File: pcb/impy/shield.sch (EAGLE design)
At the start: 119 parts, among them J1 USB-2410-06, J2 SI-60062-F, J3 5V, U1 AD5933YRS, U10 LTC3406AB, U11 23LCV1024-I/SN, U12 MIC2009A-1YM6, U13 ADG725BSU, U14 ADG725BSU, U2 ADG704BRM, U3 AD8656ARZ, U4 M24C08WMN, U5 ADG706BRU, U6 DP83848I, U7 MIC2009A-1YM6, U8 AT25DF081A-SS, U9 SST25VF080B-80-4I-S2

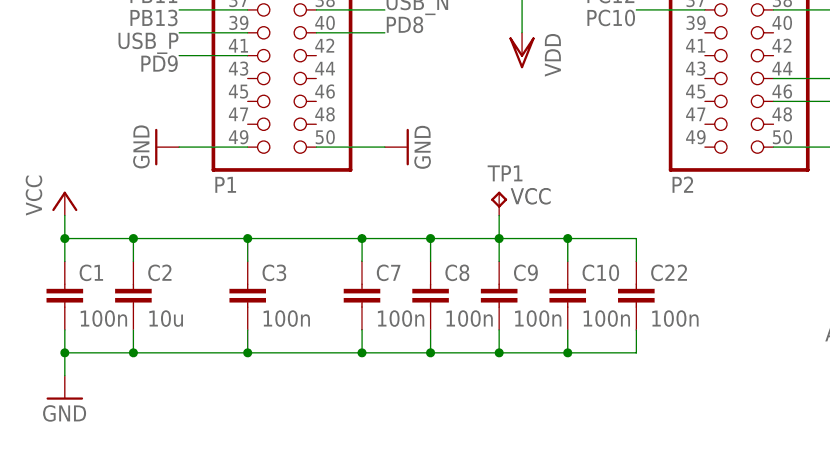
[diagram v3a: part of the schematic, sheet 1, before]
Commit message: * pcb/impy: (shield.brd) Layout USB connector.   (shield.sch) Fix wrong supply net connection for USB bypass capacitors C1 and C2 (was VCC, should be +5V).
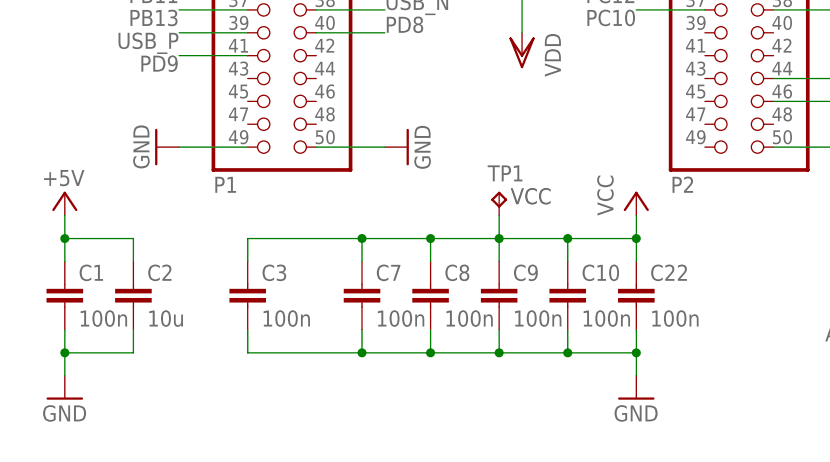
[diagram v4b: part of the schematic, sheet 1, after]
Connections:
- net +5V: now also C1.1, C2.1
- net VCC: no longer C1.1, C2.1
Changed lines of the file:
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@@
 </part>
 <part name="R20" library="rcl" deviceset="R-EU_" device="R0603" value="10k"/>
+<part name="GND44" library="supply1" deviceset="GND" device=""/>
+<part name="P+36" library="supply1" deviceset="+5V" device=""/>
 </parts>
 <sheets>
@@
 <instance part="C6" gate="G$1" x="114.3" y="5.08"/>
 <instance part="GND14" gate="1" x="0" y="-7.62"/>
-<instance part="P+12" gate="VCC" x="0" y="15.24"/>
+<instance part="P+12" gate="VCC" x="63.5" y="15.24"/>
 <instance part="P+13" gate="VCC" x="104.14" y="15.24"/>
 <instance part="AGND6" gate="VR1" x="104.14" y="-7.62"/>
@@
 <instance part="TP1" gate="G$1" x="48.26" y="15.24"/>
 <instance part="TP2" gate="G$1" x="152.4" y="25.4"/>
+<instance part="GND44" gate="1" x="63.5" y="-7.62"/>
+<instance part="P+36" gate="1" x="0" y="15.24" smashed="yes" rot="MR0">
+<attribute name="VALUE" x="-2.54" y="17.78" size="1.778" layer="96" rot="MR180"/>
+</instance>
 </instances>
 <busses>
@@
 </segment>
 <segment>
-<pinref part="C1" gate="G$1" pin="2"/>
+<pinref part="C2" gate="G$1" pin="2"/>
+<wire x1="7.62" y1="-2.54" x2="7.62" y2="0" width="0.1524" layer="91"/>
 <pinref part="GND14" gate="1" pin="GND"/>
-<wire x1="0" y1="0" x2="0" y2="-2.54" width="0.1524" layer="91"/>
-<pinref part="C2" gate="G$1" pin="2"/>
 <wire x1="0" y1="-2.54" x2="0" y2="-5.08" width="0.1524" layer="91"/>
 <wire x1="0" y1="-2.54" x2="7.62" y2="-2.54" width="0.1524" layer="91"/>
-<wire x1="7.62" y1="-2.54" x2="7.62" y2="0" width="0.1524" layer="91"/>
 <junction x="0" y="-2.54"/>
+<pinref part="C1" gate="G$1" pin="2"/>
+<wire x1="0" y1="0" x2="0" y2="-2.54" width="0.1524" layer="91"/>
+</segment>
+<segment>
 <pinref part="C3" gate="G$1" pin="2"/>
-<wire x1="7.62" y1="-2.54" x2="20.32" y2="-2.54" width="0.1524" layer="91"/>
 <wire x1="20.32" y1="-2.54" x2="20.32" y2="0" width="0.1524" layer="91"/>
-<junction x="7.62" y="-2.54"/>
 <pinref part="C7" gate="G$1" pin="2"/>
 <wire x1="20.32" y1="-2.54" x2="33.02" y2="-2.54" width="0.1524" layer="91"/>
 <wire x1="33.02" y1="-2.54" x2="33.02" y2="0" width="0.1524" layer="91"/>
-<junction x="20.32" y="-2.54"/>
 <pinref part="C8" gate="G$1" pin="2"/>
 <wire x1="33.02" y1="-2.54" x2="40.64" y2="-2.54" width="0.1524" layer="91"/>
@@
 <wire x1="63.5" y1="-2.54" x2="63.5" y2="0" width="0.1524" layer="91"/>
 <junction x="55.88" y="-2.54"/>
+<pinref part="GND44" gate="1" pin="GND"/>
+<wire x1="63.5" y1="-5.08" x2="63.5" y2="-2.54" width="0.1524" layer="91"/>
+<junction x="63.5" y="-2.54"/>
 </segment>
 <segment>
@@
 <junction x="96.52" y="78.74"/>
 </segment>
+<segment>
+<pinref part="C1" gate="G$1" pin="1"/>
+<pinref part="C2" gate="G$1" pin="1"/>
+<wire x1="7.62" y1="10.16" x2="7.62" y2="7.62" width="0.1524" layer="91"/>
+<wire x1="0" y1="10.16" x2="7.62" y2="10.16" width="0.1524" layer="91"/>
+<wire x1="0" y1="10.16" x2="0" y2="7.62" width="0.1524" layer="91"/>
+<pinref part="P+36" gate="1" pin="+5V"/>
+<wire x1="0" y1="10.16" x2="0" y2="12.7" width="0.1524" layer="91"/>
+<junction x="0" y="10.16"/>
+</segment>
 </net>
 <net name="+3V3" class="1">
@@
 <segment>
 <pinref part="P+12" gate="VCC" pin="VCC"/>
-<pinref part="C1" gate="G$1" pin="1"/>
-<wire x1="0" y1="12.7" x2="0" y2="10.16" width="0.1524" layer="91"/>
-<pinref part="C2" gate="G$1" pin="1"/>
-<wire x1="0" y1="10.16" x2="0" y2="7.62" width="0.1524" layer="91"/>
-<wire x1="0" y1="10.16" x2="7.62" y2="10.16" width="0.1524" layer="91"/>
-<wire x1="7.62" y1="10.16" x2="7.62" y2="7.62" width="0.1524" layer="91"/>
-<junction x="0" y="10.16"/>
 <pinref part="C3" gate="G$1" pin="1"/>
-<wire x1="7.62" y1="10.16" x2="20.32" y2="10.16" width="0.1524" layer="91"/>
 <wire x1="20.32" y1="10.16" x2="20.32" y2="7.62" width="0.1524" layer="91"/>
-<junction x="7.62" y="10.16"/>
 <pinref part="C7" gate="G$1" pin="1"/>
 <wire x1="20.32" y1="10.16" x2="33.02" y2="10.16" width="0.1524" layer="91"/>
 <wire x1="33.02" y1="10.16" x2="33.02" y2="7.62" width="0.1524" layer="91"/>
-<junction x="20.32" y="10.16"/>
 <pinref part="C8" gate="G$1" pin="1"/>
 <wire x1="33.02" y1="10.16" x2="40.64" y2="10.16" width="0.1524" layer="91"/>
@@
 <pinref part="TP1" gate="G$1" pin="TP"/>
 <wire x1="48.26" y1="12.7" x2="48.26" y2="10.16" width="0.1524" layer="91"/>
-</segment>
-<segment>
+<wire x1="63.5" y1="10.16" x2="63.5" y2="12.7" width="0.1524" layer="91"/>
+<junction x="63.5" y="10.16"/>
+</segment>
+<segment>

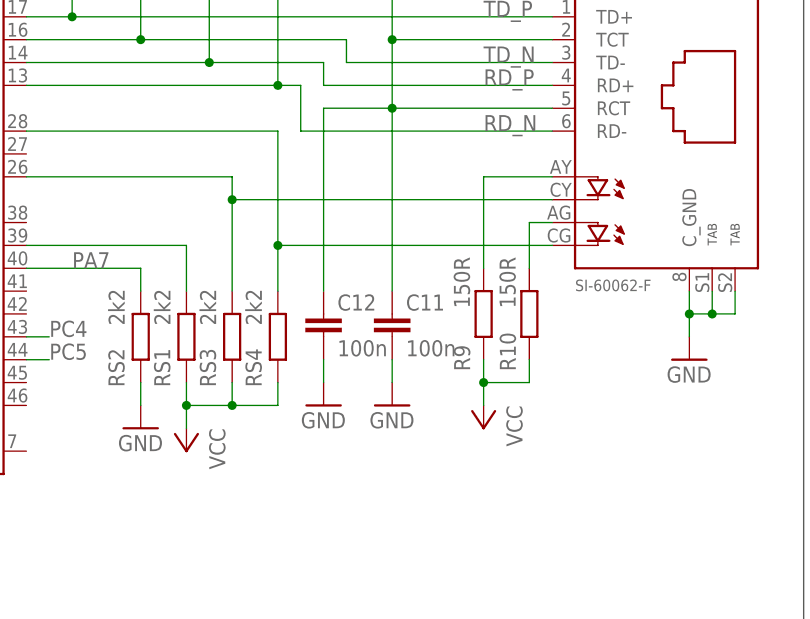
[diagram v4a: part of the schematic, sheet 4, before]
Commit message: * pcb/impy: (shield.sch) Swap around Ethernet jack LED dropper resistors for better routing.   (shield.brd) Change layout of Ethernet LEDs.
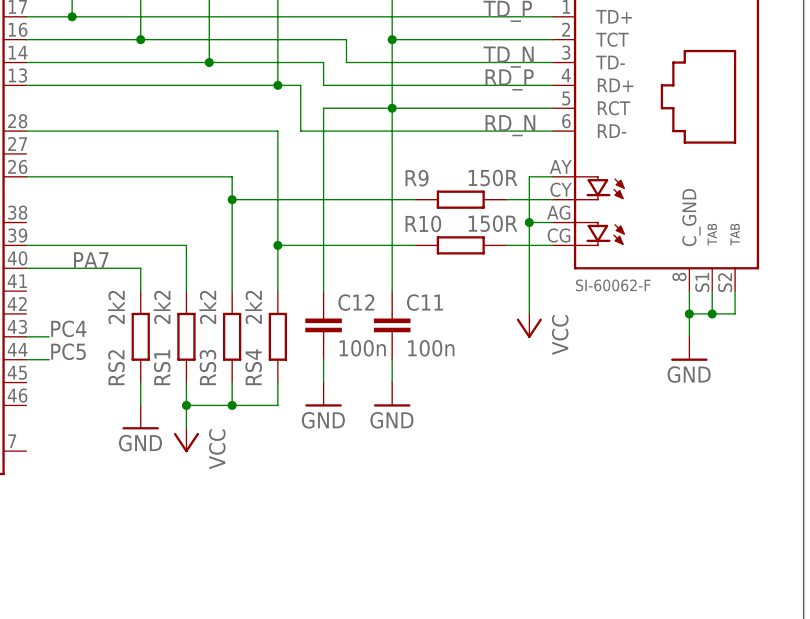
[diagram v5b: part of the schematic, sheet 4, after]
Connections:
- net N$20: now also J2.CY, R9.2; no longer J2.AG, R10.2
- net N$22: now also R9.1; no longer J2.CY
- net N$23: now also R10.1; no longer J2.CG
- net N$25: now also J2.CG, R10.2; no longer J2.AY, R9.2
- net VCC: now also J2.AG, J2.AY; no longer R10.1, R9.1
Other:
- moved on the sheet: R10, R9
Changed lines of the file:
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@@
 </instance>
 <instance part="GND30" gate="1" x="119.38" y="78.74" rot="R180"/>
-<instance part="P+23" gate="VCC" x="187.96" y="20.32" rot="R180"/>
+<instance part="P+23" gate="VCC" x="193.04" y="30.48" rot="R180"/>
 <instance part="RS3" gate="G$1" x="160.02" y="30.48" smashed="yes" rot="R90">
 <attribute name="NAME" x="156.4386" y="29.21" size="1.778" layer="95" rot="R270"/>
@@
 <attribute name="VALUE" x="163.322" y="31.75" size="1.778" layer="96" rot="R90"/>
 </instance>
-<instance part="R9" gate="G$1" x="187.96" y="33.02" smashed="yes" rot="R90">
-<attribute name="NAME" x="186.4614" y="26.67" size="1.778" layer="95" rot="R90"/>
-<attribute name="VALUE" x="184.658" y="39.37" size="1.778" layer="96" rot="R270"/>
+<instance part="R9" gate="G$1" x="185.42" y="45.72" smashed="yes">
+<attribute name="NAME" x="179.07" y="47.2186" size="1.778" layer="95"/>
+<attribute name="VALUE" x="191.77" y="49.022" size="1.778" layer="96" rot="R180"/>
 </instance>
-<instance part="R10" gate="G$1" x="193.04" y="33.02" smashed="yes" rot="R90">
-<attribute name="NAME" x="191.5414" y="26.67" size="1.778" layer="95" rot="R90"/>
-<attribute name="VALUE" x="189.738" y="39.37" size="1.778" layer="96" rot="R270"/>
+<instance part="R10" gate="G$1" x="185.42" y="40.64" smashed="yes">
+<attribute name="NAME" x="179.07" y="42.1386" size="1.778" layer="95"/>
+<attribute name="VALUE" x="191.77" y="43.942" size="1.778" layer="96" rot="R180"/>
 </instance>
 <instance part="U7" gate="G$1" x="10.16" y="35.56"/>
@@
 </segment>
 <segment>
-<pinref part="P+23" gate="VCC" pin="VCC"/>
-<pinref part="R9" gate="G$1" pin="1"/>
-<wire x1="187.96" y1="22.86" x2="187.96" y2="25.4" width="0.1524" layer="91"/>
-<pinref part="R10" gate="G$1" pin="1"/>
-<wire x1="187.96" y1="25.4" x2="187.96" y2="27.94" width="0.1524" layer="91"/>
-<wire x1="187.96" y1="25.4" x2="193.04" y2="25.4" width="0.1524" layer="91"/>
-<wire x1="193.04" y1="25.4" x2="193.04" y2="27.94" width="0.1524" layer="91"/>
-<junction x="187.96" y="25.4"/>
-</segment>
-<segment>
 <pinref part="R11" gate="G$1" pin="2"/>
 <pinref part="P+30" gate="VCC" pin="VCC"/>
 <wire x1="43.18" y1="38.1" x2="43.18" y2="40.64" width="0.1524" layer="91"/>
+</segment>
+<segment>
+<pinref part="J2" gate="G$1" pin="AY"/>
+<pinref part="P+23" gate="VCC" pin="VCC"/>
+<wire x1="195.58" y1="48.26" x2="193.04" y2="48.26" width="0.1524" layer="91"/>
+<wire x1="193.04" y1="48.26" x2="193.04" y2="43.18" width="0.1524" layer="91"/>
+<pinref part="J2" gate="G$1" pin="AG"/>
+<wire x1="193.04" y1="43.18" x2="193.04" y2="33.02" width="0.1524" layer="91"/>
+<wire x1="195.58" y1="43.18" x2="193.04" y2="43.18" width="0.1524" layer="91"/>
+<junction x="193.04" y="43.18"/>
 </segment>
 </net>
@@
 <wire x1="137.16" y1="48.26" x2="160.02" y2="48.26" width="0.1524" layer="91"/>
 <wire x1="160.02" y1="48.26" x2="160.02" y2="45.72" width="0.1524" layer="91"/>
-<pinref part="J2" gate="G$1" pin="CY"/>
+<pinref part="R9" gate="G$1" pin="1"/>
 <wire x1="160.02" y1="45.72" x2="160.02" y2="35.56" width="0.1524" layer="91"/>
-<wire x1="195.58" y1="45.72" x2="160.02" y2="45.72" width="0.1524" layer="91"/>
+<wire x1="180.34" y1="45.72" x2="160.02" y2="45.72" width="0.1524" layer="91"/>
 <junction x="160.02" y="45.72"/>
 </segment>
@@
 <wire x1="137.16" y1="53.34" x2="165.1" y2="53.34" width="0.1524" layer="91"/>
 <wire x1="165.1" y1="53.34" x2="165.1" y2="40.64" width="0.1524" layer="91"/>
-<pinref part="J2" gate="G$1" pin="CG"/>
+<pinref part="R10" gate="G$1" pin="1"/>
 <wire x1="165.1" y1="40.64" x2="165.1" y2="35.56" width="0.1524" layer="91"/>
-<wire x1="195.58" y1="40.64" x2="165.1" y2="40.64" width="0.1524" layer="91"/>
+<wire x1="180.34" y1="40.64" x2="165.1" y2="40.64" width="0.1524" layer="91"/>
 <junction x="165.1" y="40.64"/>
-</segment>
-</net>
-<net name="N$20" class="0">
-<segment>
-<pinref part="J2" gate="G$1" pin="AG"/>
-<pinref part="R10" gate="G$1" pin="2"/>
-<wire x1="195.58" y1="43.18" x2="193.04" y2="43.18" width="0.1524" layer="91"/>
-<wire x1="193.04" y1="43.18" x2="193.04" y2="38.1" width="0.1524" layer="91"/>
-</segment>
-</net>
-<net name="N$25" class="0">
-<segment>
-<pinref part="J2" gate="G$1" pin="AY"/>
-<pinref part="R9" gate="G$1" pin="2"/>
-<wire x1="195.58" y1="48.26" x2="187.96" y2="48.26" width="0.1524" layer="91"/>
-<wire x1="187.96" y1="48.26" x2="187.96" y2="38.1" width="0.1524" layer="91"/>
 </segment>
 </net>
@@
 </segment>
 </net>
+<net name="N$20" class="0">
+<segment>
+<pinref part="R9" gate="G$1" pin="2"/>
+<pinref part="J2" gate="G$1" pin="CY"/>
+<wire x1="190.5" y1="45.72" x2="195.58" y2="45.72" width="0.1524" layer="91"/>
+</segment>
+</net>
+<net name="N$25" class="0">
+<segment>
+<pinref part="J2" gate="G$1" pin="CG"/>
+<pinref part="R10" gate="G$1" pin="2"/>
+<wire x1="195.58" y1="40.64" x2="190.5" y2="40.64" width="0.1524" layer="91"/>
+</segment>
+</net>

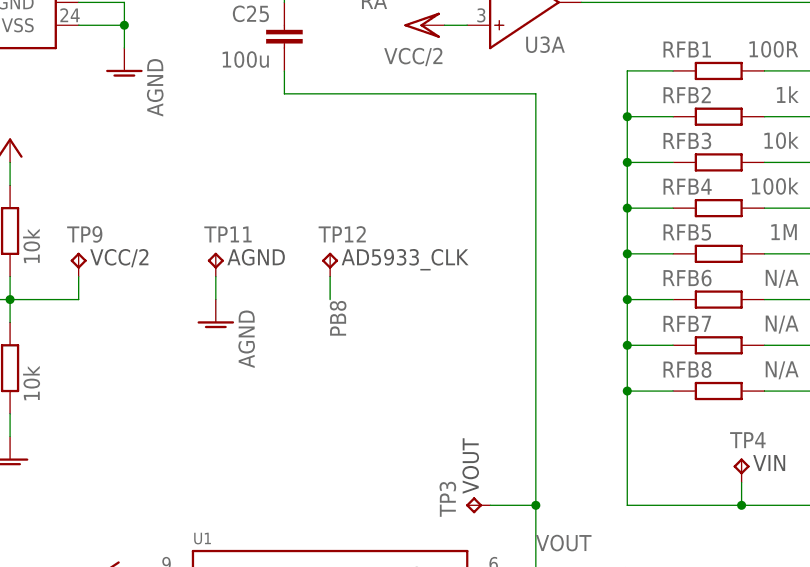
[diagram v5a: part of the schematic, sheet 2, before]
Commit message: * pcb/impy: (shield.brd) Layout most of the AD5933 related circuit.   (shield.sch) Remove unnecessary AD5933 clock signal test pad (TP12), is accessible from the discovery board anyway.
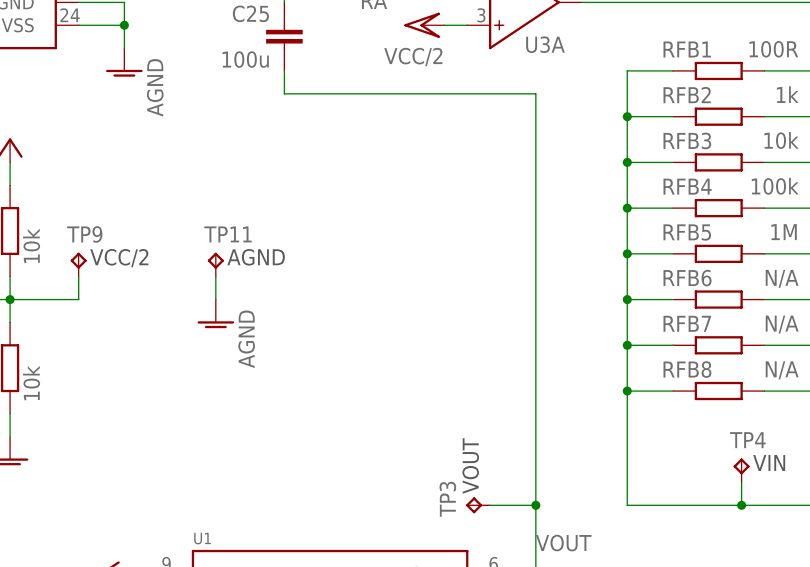
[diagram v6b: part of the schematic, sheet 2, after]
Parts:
- removed TP12: TPTP20R, testpad:TPTP20R
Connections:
- net PB8: no longer TP12.TP
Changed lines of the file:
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@@
 <attribute name="TP_SIGNAL_NAME" value="MAC_CLK"/>
-</part>
-<part name="TP12" library="testpad" deviceset="TP" device="TP20R">
-<attribute name="TP_SIGNAL_NAME" value="AD5933_CLK"/>
 </part>
 <part name="R20" library="rcl" deviceset="R-EU_" device="R0603" value="10k"/>
@@
 <instance part="TP11" gate="G$1" x="35.56" y="88.9"/>
 <instance part="AGND14" gate="VR1" x="35.56" y="81.28" rot="MR0"/>
-<instance part="TP12" gate="G$1" x="48.26" y="88.9"/>
 <instance part="R20" gate="G$1" x="147.32" y="58.42"/>
 </instances>
@@
 <label x="22.86" y="40.64" size="1.778" layer="95" rot="R180"/>
 </segment>
-<segment>
-<pinref part="TP12" gate="G$1" pin="TP"/>
-<wire x1="48.26" y1="86.36" x2="48.26" y2="83.82" width="0.1524" layer="91"/>
-<label x="48.26" y="83.82" size="1.778" layer="95" rot="R270"/>
-</segment>
-</net>
+</net>

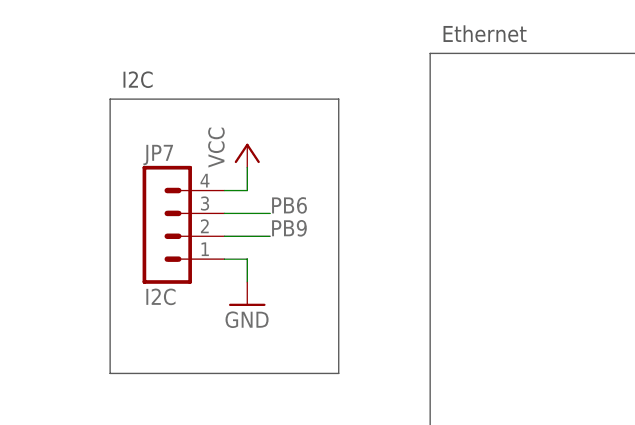
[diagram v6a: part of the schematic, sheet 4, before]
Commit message: * pcb/impy: (shield.sch) Fix supply of I2C header, should be VDD in case this is supplied from the discovery board or does not match VCC for some other reason.
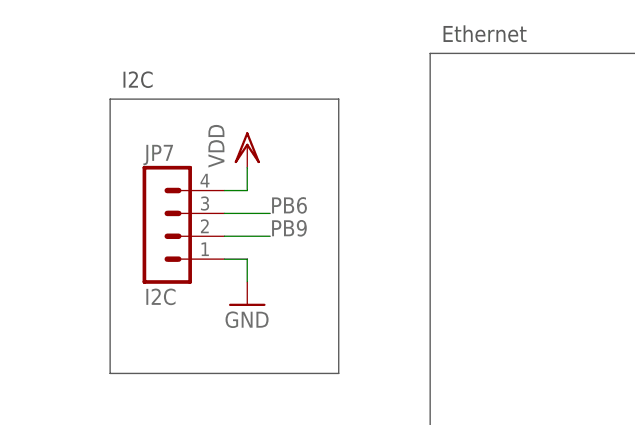
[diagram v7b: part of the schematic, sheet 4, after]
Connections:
- net VCC: no longer JP7.4
- net VDD: now also JP7.4
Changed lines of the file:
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@@
 <part name="JP7" library="con-lstb" deviceset="MA04-1" device="" value="I2C"/>
 <part name="GND16" library="supply1" deviceset="GND" device=""/>
-<part name="P+15" library="supply1" deviceset="VCC" device=""/>
 <part name="U6" library="parts" deviceset="DP83848" device="" technology="I"/>
 <part name="C7" library="rcl" deviceset="C-EU" device="C0603" value="100n"/>
@@
 <part name="GND44" library="supply1" deviceset="GND" device=""/>
 <part name="P+36" library="supply1" deviceset="+5V" device=""/>
+<part name="VDD7" library="supply1" deviceset="VDD" device=""/>
 </parts>
 <sheets>
@@
 <instance part="JP7" gate="1" x="5.08" y="81.28"/>
 <instance part="GND16" gate="1" x="15.24" y="71.12"/>
-<instance part="P+15" gate="VCC" x="15.24" y="88.9"/>
 <instance part="U6" gate="G$1" x="104.14" y="43.18"/>
 <instance part="J2" gate="G$1" x="208.28" y="53.34"/>
@@
 </instance>
 <instance part="TP14" gate="G$1" x="88.9" y="7.62" rot="R180"/>
+<instance part="VDD7" gate="G$1" x="15.24" y="88.9"/>
 </instances>
 <busses>
@@
 <net name="VCC" class="1">
 <segment>
-<pinref part="JP7" gate="1" pin="4"/>
-<pinref part="P+15" gate="VCC" pin="VCC"/>
-<wire x1="12.7" y1="83.82" x2="15.24" y2="83.82" width="0.1524" layer="91"/>
-<wire x1="15.24" y1="83.82" x2="15.24" y2="86.36" width="0.1524" layer="91"/>
-</segment>
-<segment>
 <pinref part="P+18" gate="VCC" pin="VCC"/>
 <wire x1="177.8" y1="68.58" x2="177.8" y2="63.5" width="0.1524" layer="91"/>
@@
 </segment>
 </net>
+<net name="VDD" class="1">
+<segment>
+<pinref part="JP7" gate="1" pin="4"/>
+<wire x1="12.7" y1="83.82" x2="15.24" y2="83.82" width="0.1524" layer="91"/>
+<wire x1="15.24" y1="83.82" x2="15.24" y2="86.36" width="0.1524" layer="91"/>
+<pinref part="VDD7" gate="G$1" pin="VDD"/>
+</segment>
+</net>
